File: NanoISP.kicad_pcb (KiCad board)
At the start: 2 copper layers, 54 x 38.1 mm, 12 parts, among them J1 Conn_02x03_Odd_Even

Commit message: No more DRC issues. Wider via.
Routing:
- net Net-(D3-Pad2): track 43.4 -> 42.8 mm
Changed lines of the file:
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@@
     (pad_to_mask_clearance 0)
     (aux_axis_origin 106.045 27.94)
-    (grid_origin 106.045 27.94)
     (pcbplotparams
       (layerselection 0x0001000_fffffffe)
@@
   (segment (start 118.11 43.18) (end 114.935 40.005) (width 0.8) (layer "B.Cu") (net 12))
   (segment (start 151.765 43.18) (end 151.765 47.625) (width 0.8) (layer "F.Cu") (net 13))
-  (via (at 151.765 47.625) (size 1.2) (drill 0.4) (layers "F.Cu" "B.Cu") (net 13))
-  (via (at 151.765 43.18) (size 1.2) (drill 0.4) (layers "F.Cu" "B.Cu") (net 13))
+  (via (at 151.765 43.18) (size 1.85) (drill 0.7) (layers "F.Cu" "B.Cu") (net 13))
+  (via (at 151.765 47.625) (size 1.85) (drill 0.7) (layers "F.Cu" "B.Cu") (net 13))
   (segment (start 120.015 47.625) (end 115.57 43.18) (width 0.8) (layer "B.Cu") (net 13))
-  (segment (start 151.765 43.18) (end 157.48 48.26) (width 0.8) (layer "B.Cu") (net 13))
   (segment (start 151.765 47.625) (end 120.015 47.625) (width 0.8) (layer "B.Cu") (net 13))
+  (segment (start 152.4 43.18) (end 157.48 48.26) (width 0.8) (layer "B.Cu") (net 13))
+  (segment (start 151.765 43.18) (end 152.4 43.18) (width 0.8) (layer "B.Cu") (net 13))
   (segment (start 113.03 43.18) (end 120.65 50.8) (width 0.8) (layer "B.Cu") (net 14))
   (segment (start 120.65 50.8) (end 154.94 50.8) (width 0.8) (layer "B.Cu") (net 14))
   (segment (start 151.765 58.42) (end 151.765 53.34) (width 0.8) (layer "F.Cu") (net 15))
-  (via (at 151.765 58.42) (size 1.2) (drill 0.4) (layers "F.Cu" "B.Cu") (net 15))
-  (via (at 151.765 53.34) (size 1.2) (drill 0.4) (layers "F.Cu" "B.Cu") (net 15))
+  (via (at 151.765 58.42) (size 1.85) (drill 0.7) (layers "F.Cu" "B.Cu") (net 15))
+  (via (at 151.765 53.34) (size 1.85) (drill 0.7) (layers "F.Cu" "B.Cu") (net 15))
   (segment (start 157.48 53.34) (end 151.765 58.42) (width 0.8) (layer "B.Cu") (net 15))
   (segment (start 120.65 53.34) (end 110.49 43.18) (width 0.8) (layer "B.Cu") (net 15))
@@
   (segment (start 153.67 60.325) (end 112.395 60.325) (width 0.8) (layer "B.Cu") (net 16))
   (segment (start 158.682081 50.8) (end 159.385 51.502919) (width 0.8) (layer "B.Cu") (net 16))
-  (segment (start 149.86 58.42) (end 146.05 58.42) (width 0.8) (layer "B.Cu") (net 29))
-  (segment (start 154.94 53.34) (end 149.86 58.42) (width 0.8) (layer "B.Cu") (net 29))
+  (segment (start 154.94 53.34) (end 149.225 58.42) (width 0.8) (layer "B.Cu") (net 29))
+  (segment (start 149.225 58.42) (end 146.05 58.42) (width 0.8) (layer "B.Cu") (net 29))
   (segment (start 130.81 32.385) (end 133.985 35.56) (width 0.8) (layer "B.Cu") (net 30))
   (segment (start 126.365 32.385) (end 130.81 32.385) (width 0.8) (layer "B.Cu") (net 30))
@@
   (segment (start 120.015 32.385) (end 121.464511 30.935489) (width 0.8) (layer "B.Cu") (net 31))
   (segment (start 121.464511 30.935489) (end 138.885489 30.935489) (width 0.8) (layer "B.Cu") (net 31))
-  (segment (start 153.035 35.56) (end 153.035 34.925) (width 0.6) (layer "B.Cu") (net 32))
   (segment (start 116.164031 29.885969) (end 147.360969 29.885969) (width 0.8) (layer "B.Cu") (net 32))
   (segment (start 147.360969 29.885969) (end 153.035 35.56) (width 0.8) (layer "B.Cu") (net 32))

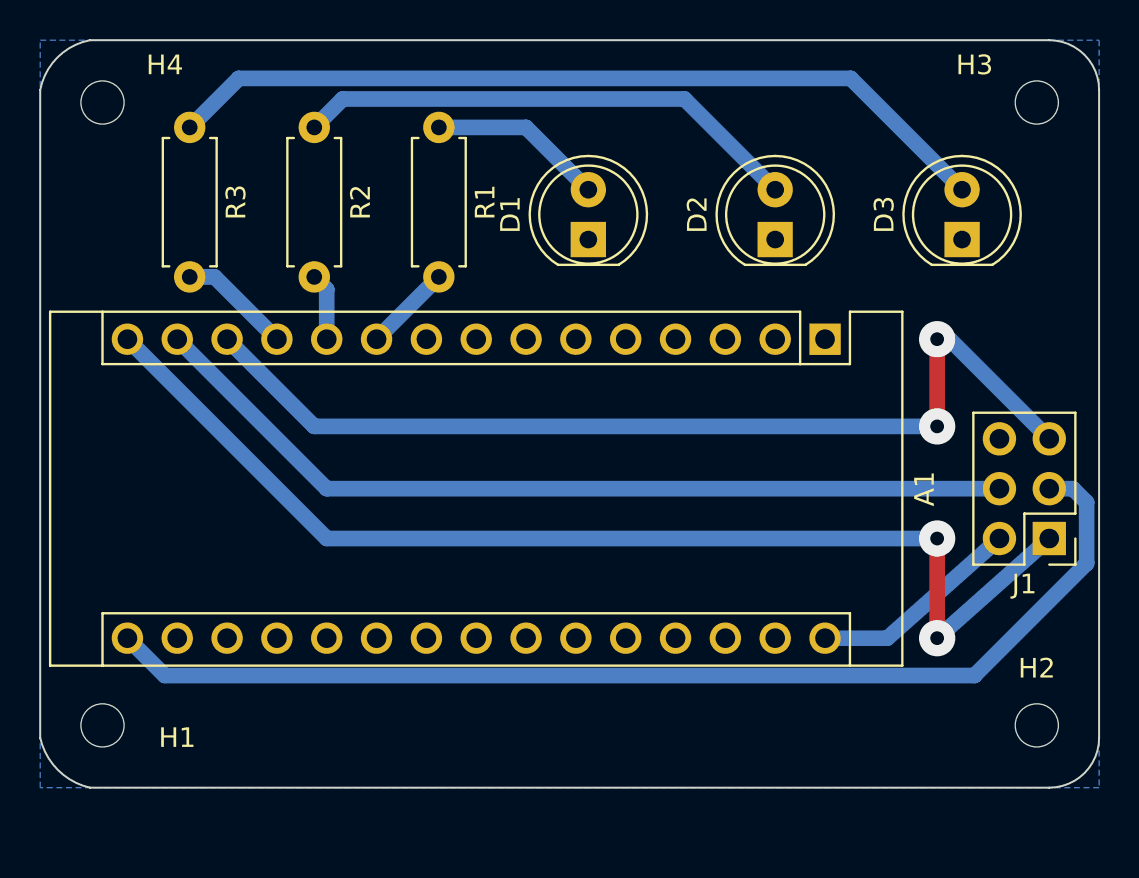
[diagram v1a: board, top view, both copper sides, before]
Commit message: Inverse plot.
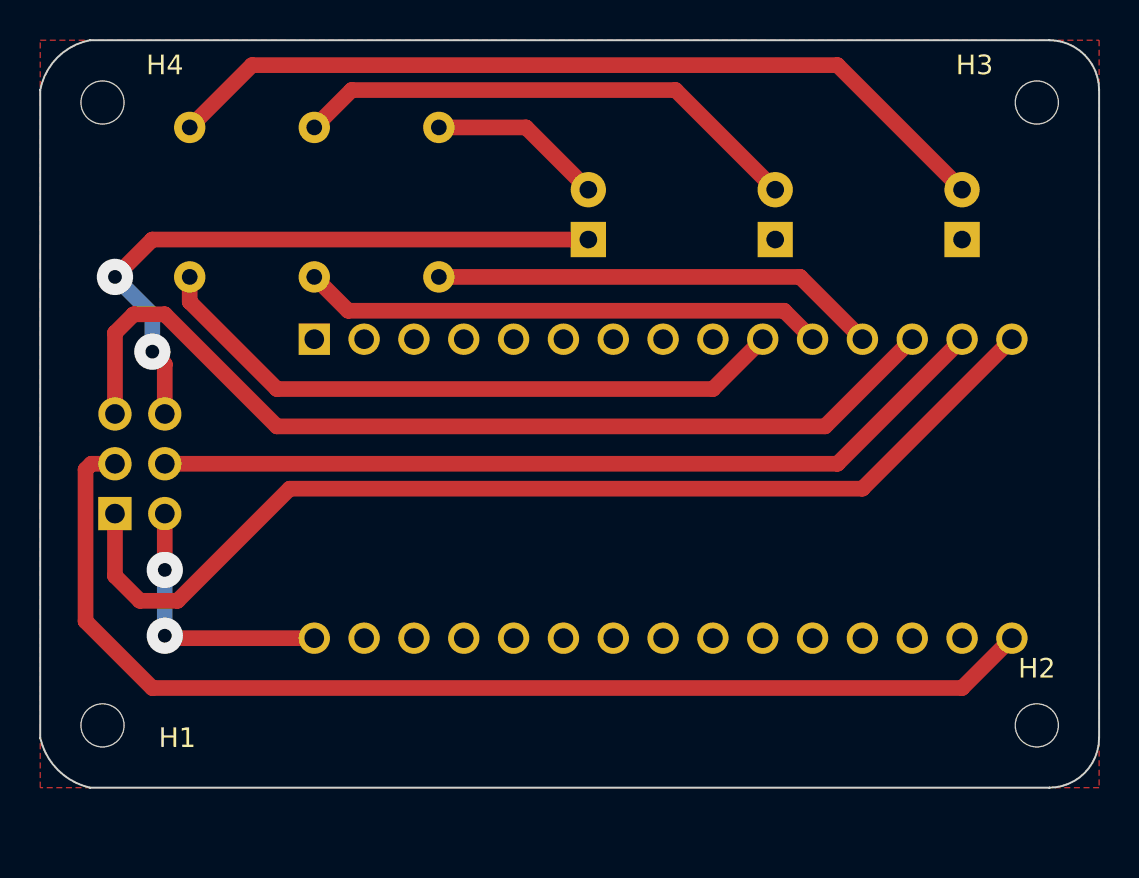
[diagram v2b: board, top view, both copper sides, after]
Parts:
- A1, D1, D2, D3, J1, R1, R2, R3: moved to B.Cu
- moved J1 47.6 mm to (109.9, 52.1), turned to 0 degrees
- moved A1 26.0 mm to (120.0, 43.2)
- moved D1 19.0 mm to (153.0, 38.1)
- moved D3 19.0 mm to (134.0, 38.1)
- moved R1 12.7 mm to (113.7, 32.4)
- moved R3 12.7 mm to (126.4, 32.4)
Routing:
- net Net-(D1-Pad2): track 8.94 -> 43.3 mm
- net Net-(D3-Pad2): track 42.8 -> 8.94 mm
- net /GND: track 0.00 -> 33.0 mm, vias 0 -> 2
- net Net-(A1-Pad10): track 4.49 -> 33.4 mm
- net Net-(A1-Pad11): track 3.44 -> 26.7 mm
- net Net-(A1-Pad12): track 5.76 -> 22.9 mm
- net Net-(A1-Pad15): track 58.2 -> 54.9 mm, vias 2 -> 0
- net Net-(A1-Pad30): track 10.8 -> 13.9 mm, vias 0 -> 2
- net Net-(A1-Pad14): track 45.1 -> 43.3 mm
- net Net-(A1-Pad16): track 57.4 -> 59.0 mm
- net Net-(A1-Pad13): track 50.3 -> 49.4 mm, vias 2 -> 0
- added copper zone on F.Cu, net /GND
- removed copper zone on B.Cu, net /GND

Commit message: Added the capacitor for handling ready / unready.
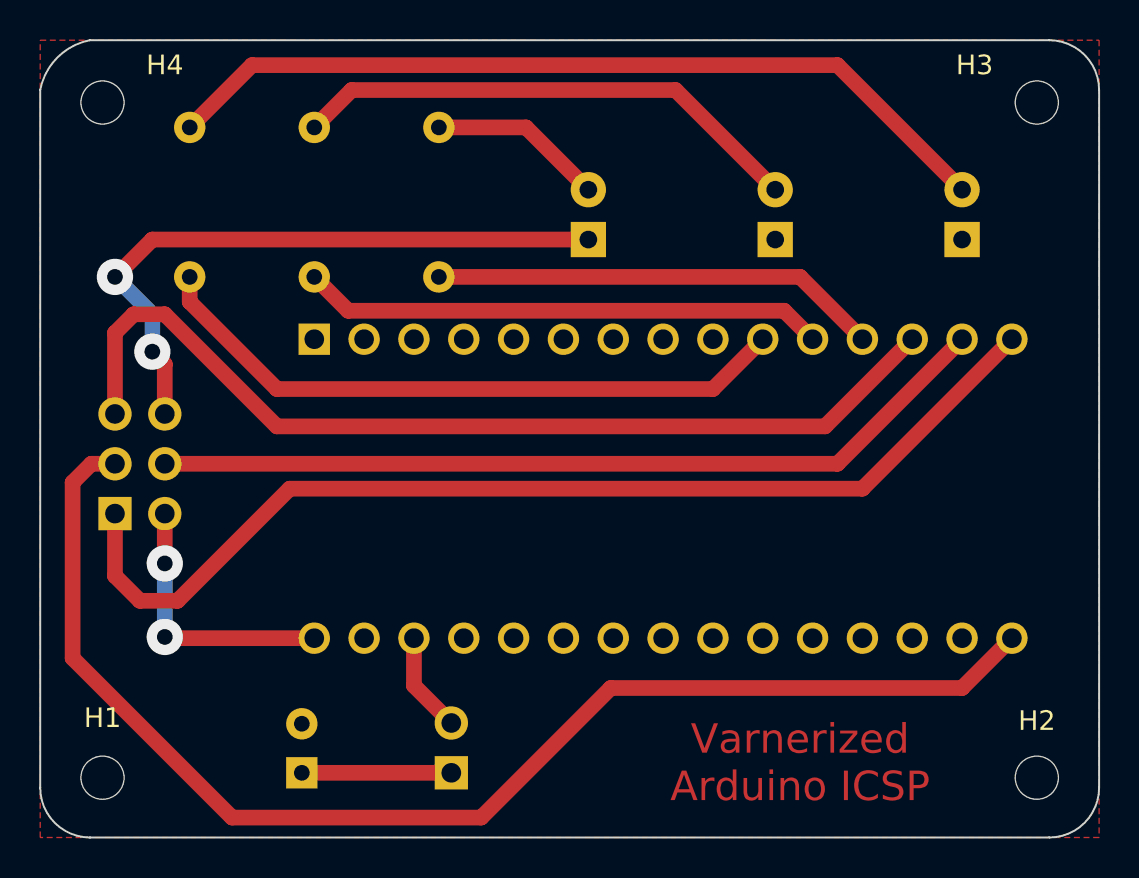
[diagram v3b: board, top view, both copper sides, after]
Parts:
- added C1: C_Polarized, Capacitor_THT:CP_Radial_D5.0mm_P2.50mm, B.Cu at (119.4, 65.3)
- added J2: Conn_01x02_Male, Connector_PinHeader_2.54mm:PinHeader_1x02_P2.54mm_Vertical, B.Cu at (127.0, 65.3)
- moved H1 2.67 mm to (109.2, 65.5)
- moved H2 2.67 mm to (156.8, 65.5)
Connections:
- A1 pad 28: unconnected-(A1-Pad28) -> Net-(A1-Pad28)
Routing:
- net Net-(C1-Pad1): track 0.00 -> 7.65 mm
- net Net-(A1-Pad16): track 59.0 -> 66.5 mm
- net Net-(A1-Pad28): track 0.00 -> 5.11 mm
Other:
- board size 54 x 38.1 mm -> 54 x 40.6 mm
- board text added: "Varnerized Arduino ICSP"
